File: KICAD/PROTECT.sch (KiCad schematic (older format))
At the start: 13 parts, among them Q10 BC857, Q11 SQM120, Q9 SQM120

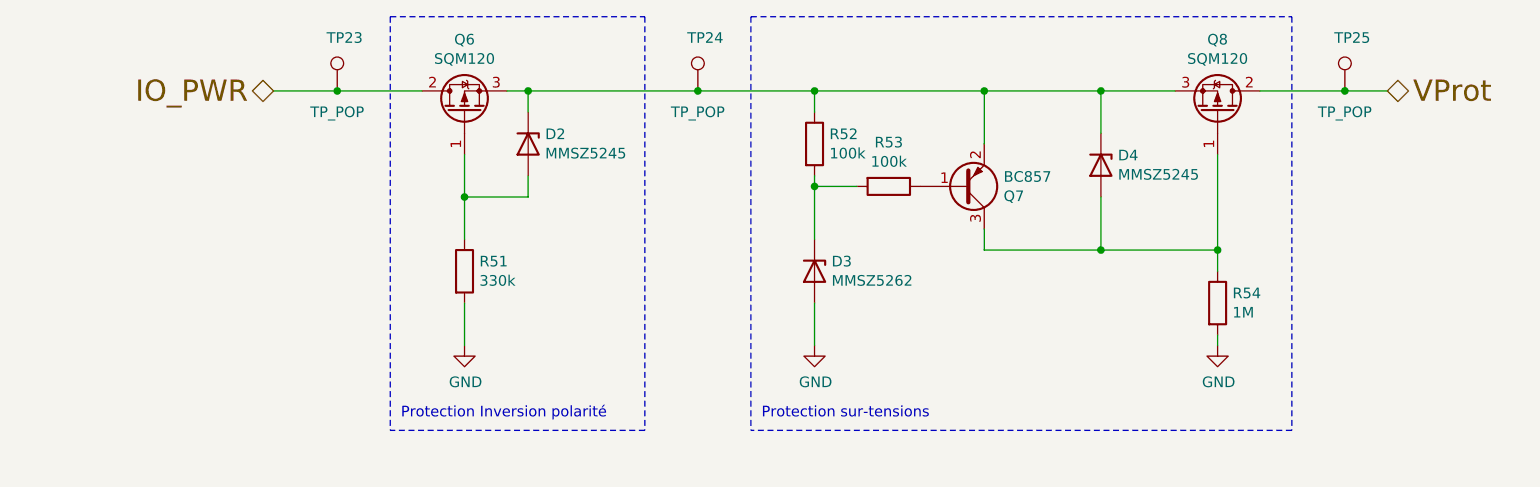
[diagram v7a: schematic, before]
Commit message: added footprint for sepic coil + no more errors in netlist
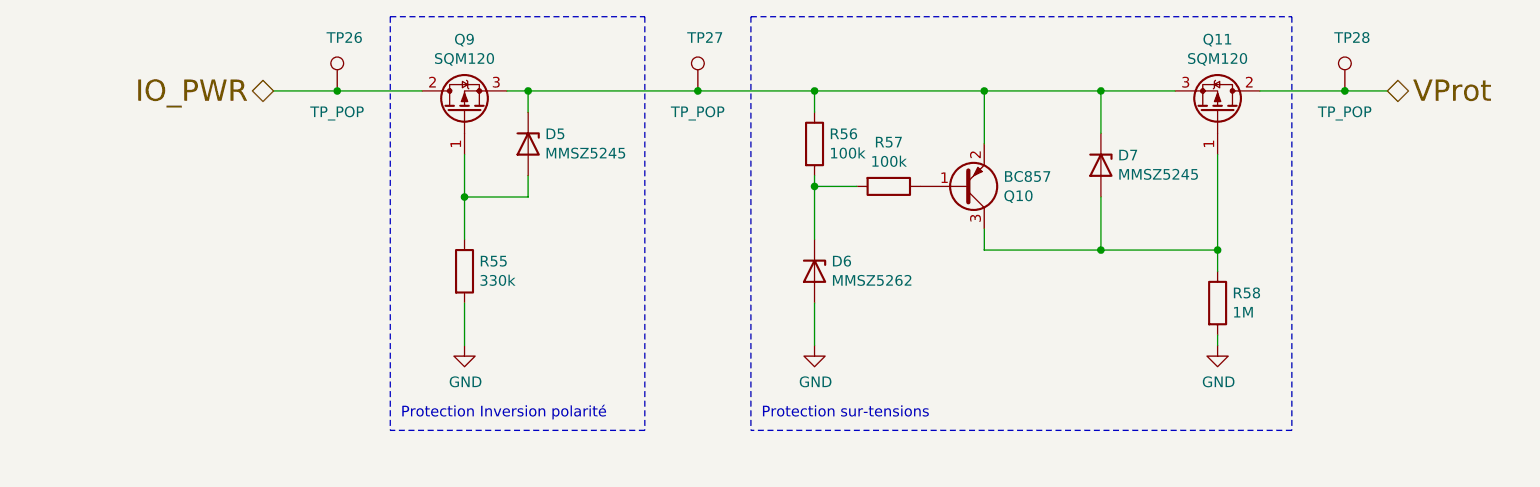
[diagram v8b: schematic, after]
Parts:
- R55, R56, R57, R58: footprint Resistor_SMD:R_0805_2012Metric_Pad1.15x1.40mm_HandSolder -> Sesame_footprint:R_0805_2012Metric_Pad1.20x1.40mm_HandSolder
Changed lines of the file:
@@
 AR Path="/61456C6A/610FCCAA" Ref="Q6"  Part="1"
 AR Path="/618D2416/610FCCAA" Ref="Q?"  Part="1"
-F 0 "Q6" V 4592 2950 50  0000 C CNN
+F 0 "Q9" V 4592 2950 50  0000 C CNN
 F 1 "SQM120" V 4501 2950 50  0000 C CNN
 F 2 "Package_TO_SOT_SMD:TO-263-2" H 4450 3050 50  0001 C CNN
@@
 AR Path="/61456C6A/610FED91" Ref="Q8"  Part="1"
 AR Path="/618D2416/610FED91" Ref="Q?"  Part="1"
-F 0 "Q8" V 8142 2950 50  0000 C CNN
+F 0 "Q11" V 8142 2950 50  0000 C CNN
 F 1 "SQM120" V 8051 2950 50  0000 C CNN
 F 2 "Package_TO_SOT_SMD:TO-263-2" H 8000 3050 50  0001 C CNN
@@
 AR Path="/61456C6A/61100A0F" Ref="D2"  Part="1"
 AR Path="/618D2416/61100A0F" Ref="D?"  Part="1"
-F 0 "D2" V 4504 3180 50  0000 L CNN
+F 0 "D5" V 4504 3180 50  0000 L CNN
 F 1 "MMSZ5245" V 4595 3180 50  0000 L CNN
 F 2 "Diode_SMD:D_SOD-123" H 4550 3100 50  0001 C CNN
@@
 AR Path="/61456C6A/61102FC8" Ref="R51"  Part="1"
 AR Path="/618D2416/61102FC8" Ref="R?"  Part="1"
-F 0 "R51" H 4320 3746 50  0000 L CNN
+F 0 "R55" H 4320 3746 50  0000 L CNN
 F 1 "330k" H 4320 3655 50  0000 L CNN
-F 2 "Resistor_SMD:R_0805_2012Metric_Pad1.15x1.40mm_HandSolder" V 4180 3700 50  0001 C CNN
+F 2 "Sesame_footprint:R_0805_2012Metric_Pad1.20x1.40mm_HandSolder" V 4180 3700 50  0001 C CNN
 F 3 "~" H 4250 3700 50  0001 C CNN
 	1    4250 3700
@@
 AR Path="/61456C6A/6110710F" Ref="Q7"  Part="1"
 AR Path="/618D2416/6110710F" Ref="Q?"  Part="1"
-F 0 "Q7" H 6791 3346 50  0000 L CNN
+F 0 "Q10" H 6791 3346 50  0000 L CNN
 F 1 "BC857" H 6791 3255 50  0000 L CNN
 F 2 "Package_TO_SOT_SMD:SOT-23" H 6800 3225 50  0001 L CIN
@@
 AR Path="/61456C6A/61107DEE" Ref="D4"  Part="1"
 AR Path="/618D2416/61107DEE" Ref="D?"  Part="1"
-F 0 "D4" V 7204 3280 50  0000 L CNN
+F 0 "D7" V 7204 3280 50  0000 L CNN
 F 1 "MMSZ5245" V 7295 3280 50  0000 L CNN
 F 2 "Diode_SMD:D_SOD-123" H 7250 3200 50  0001 C CNN
@@
 AR Path="/61456C6A/611083FB" Ref="R52"  Part="1"
 AR Path="/618D2416/611083FB" Ref="R?"  Part="1"
-F 0 "R52" H 5970 3146 50  0000 L CNN
+F 0 "R56" H 5970 3146 50  0000 L CNN
 F 1 "100k" H 5970 3055 50  0000 L CNN
-F 2 "Resistor_SMD:R_0805_2012Metric_Pad1.15x1.40mm_HandSolder" V 5830 3100 50  0001 C CNN
+F 2 "Sesame_footprint:R_0805_2012Metric_Pad1.20x1.40mm_HandSolder" V 5830 3100 50  0001 C CNN
 F 3 "~" H 5900 3100 50  0001 C CNN
 	1    5900 3100
@@
 AR Path="/61456C6A/6110B925" Ref="R53"  Part="1"
 AR Path="/618D2416/6110B925" Ref="R?"  Part="1"
-F 0 "R53" V 6043 3300 50  0000 C CNN
+F 0 "R57" V 6043 3300 50  0000 C CNN
 F 1 "100k" V 6134 3300 50  0000 C CNN
-F 2 "Resistor_SMD:R_0805_2012Metric_Pad1.15x1.40mm_HandSolder" V 6180 3300 50  0001 C CNN
+F 2 "Sesame_footprint:R_0805_2012Metric_Pad1.20x1.40mm_HandSolder" V 6180 3300 50  0001 C CNN
 F 3 "~" H 6250 3300 50  0001 C CNN
 	1    6250 3300
@@
 AR Path="/61456C6A/61115761" Ref="R54"  Part="1"
 AR Path="/618D2416/61115761" Ref="R?"  Part="1"
-F 0 "R54" H 7870 3896 50  0000 L CNN
+F 0 "R58" H 7870 3896 50  0000 L CNN
 F 1 "1M" H 7870 3805 50  0000 L CNN
-F 2 "Resistor_SMD:R_0805_2012Metric_Pad1.15x1.40mm_HandSolder" V 7730 3850 50  0001 C CNN
+F 2 "Sesame_footprint:R_0805_2012Metric_Pad1.20x1.40mm_HandSolder" V 7730 3850 50  0001 C CNN
 F 3 "~" H 7800 3850 50  0001 C CNN
 	1    7800 3850
@@
 AR Path="/61456C6A/61107C25" Ref="D3"  Part="1"
 AR Path="/618D2416/61107C25" Ref="D?"  Part="1"
-F 0 "D3" V 5854 3780 50  0000 L CNN
+F 0 "D6" V 5854 3780 50  0000 L CNN
 F 1 "MMSZ5262" V 5945 3780 50  0000 L CNN
 F 2 "Diode_SMD:D_SOD-123" H 5900 3700 50  0001 C CNN
@@
 AR Path="/61456C6A/612D3587" Ref="TP24"  Part="1"
 AR Path="/618D2416/612D3587" Ref="TP?"  Part="1"
-F 0 "TP24" H 5300 3100 50  0000 L CNN
+F 0 "TP27" H 5300 3100 50  0000 L CNN
 F 1 "TP_POP" H 5350 2750 50  0000 C CNN
 F 2 "TestPoint:TestPoint_Loop_D1.80mm_Drill1.0mm_Beaded" H 5550 2850 50  0001 C CNN
@@
 AR Path="/61456C6A/612DA888" Ref="TP25"  Part="1"
 AR Path="/618D2416/612DA888" Ref="TP?"  Part="1"
-F 0 "TP25" H 8350 3100 50  0000 L CNN
+F 0 "TP28" H 8350 3100 50  0000 L CNN
 F 1 "TP_POP" H 8400 2750 50  0000 C CNN
 F 2 "TestPoint:TestPoint_Loop_D1.80mm_Drill1.0mm_Beaded" H 8600 2850 50  0001 C CNN
@@
 AR Path="/61456C6A/614EA2DB" Ref="TP23"  Part="1"
 AR Path="/618D2416/614EA2DB" Ref="TP?"  Part="1"
-F 0 "TP23" H 3600 3100 50  0000 L CNN
+F 0 "TP26" H 3600 3100 50  0000 L CNN
 F 1 "TP_POP" H 3650 2750 50  0000 C CNN
 F 2 "TestPoint:TestPoint_Loop_D1.80mm_Drill1.0mm_Beaded" H 3850 2850 50  0001 C CNN
